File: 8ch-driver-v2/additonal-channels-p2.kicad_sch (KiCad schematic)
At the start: 42 parts, among them Q1 2N7002E, U1 DRV104PWP

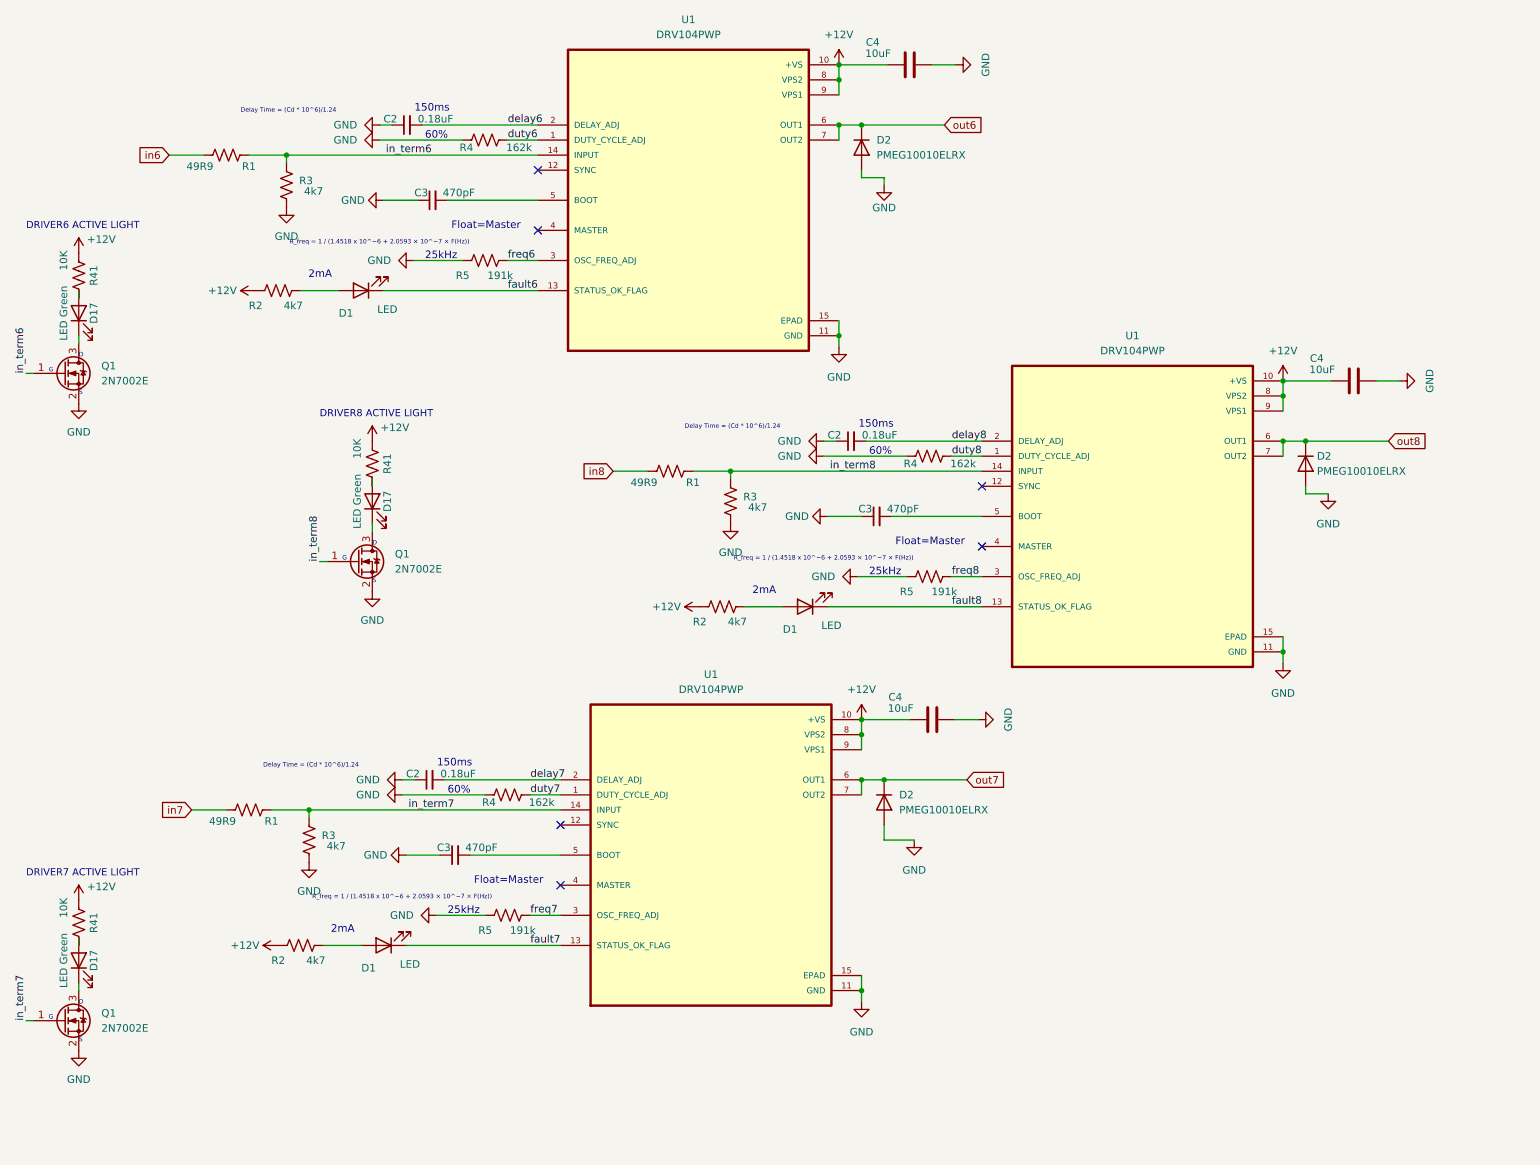
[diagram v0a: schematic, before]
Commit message: added 8 more channels and an FTDH chip
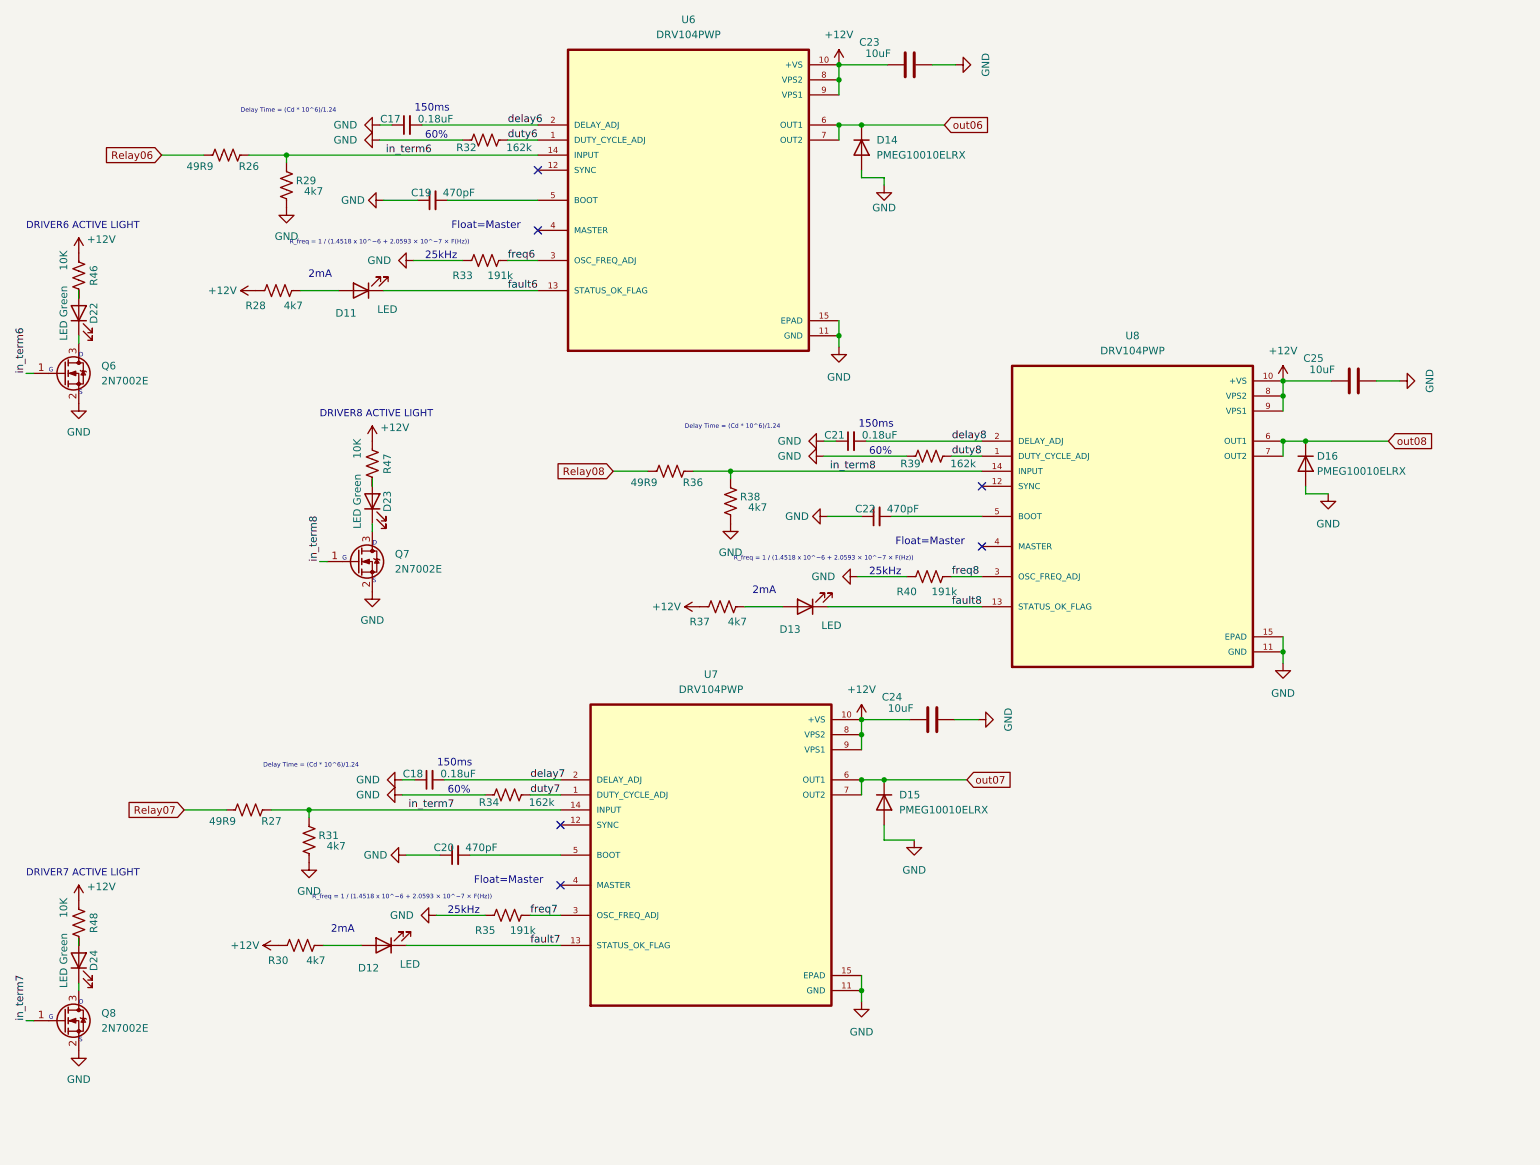
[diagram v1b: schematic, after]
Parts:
- renumbered C2 to C17, C2 to C18, C3 to C19, C3 to C20, C2 to C21, C3 to C22, C4 to C23, C4 to C24, C4 to C25, D1 to D11, D1 to D12, D1 to D13, D2 to D14, D2 to D15, D2 to D16, D17 to D22, D17 to D23, D17 to D24, Q1 to Q6, Q1 to Q7, Q1 to Q8, R1 to R26, R1 to R27, R2 to R28, R3 to R29, R2 to R30, R3 to R31, R4 to R32, R5 to R33, R4 to R34, R5 to R35, R1 to R36, R2 to R37, R3 to R38, R4 to R39, R5 to R40, R41 to R46, R41 to R47, R41 to R48, U1 to U6, U1 to U7, U1 to U8
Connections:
- net in6 renamed Relay06
- net in7 renamed Relay07
- net in8 renamed Relay08
- net out6 renamed out06
- net out7 renamed out07
- net out8 renamed out08
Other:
- title: (none) -> 16 Channel PWM Solenoid Driver - USB

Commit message: progress
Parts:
- removed C19, C22: 470pF, Capacitor_SMD:C_1206_3216Metric, symbol Device:C_Small
- removed C23, C24: 10uF, Capacitor_SMD:C_1210_3225Metric, symbol Device:C
- removed D12: LED, LED_SMD:LED_0805_2012Metric, symbol Device:LED
- removed D15: PMEG10010ELRX, Diode_SMD:Nexperia_CFP3_SOD-123W, symbol Device:D
- added C19, C22: 10uF, Capacitor_SMD:C_1210_3225Metric, symbol Device:C
- added C23: 0.18uF, Capacitor_SMD:C_1206_3216Metric, symbol Device:C_Small
- added C24: 470pF, Capacitor_SMD:C_1206_3216Metric, symbol Device:C_Small
- added D12: PMEG10010ELRX, Diode_SMD:Nexperia_CFP3_SOD-123W, symbol Device:D
- added D15: LED, LED_SMD:LED_0805_2012Metric, symbol Device:LED
- C18, C21: value 0.18uF -> 470pF; Mfg KYOCERA AVX -> Kemet; PartNum 08053C184KAT2A -> C0805C471K5RAC7800
- C20: value 470pF -> 0.18uF; Mfg Kemet -> KYOCERA AVX; PartNum C0805C471K5RAC7800 -> 08053C184KAT2A
- R27: value 49R9 -> 4k7; PartNum RC0805FR-0749R9L -> RC0805JR-074K7L
- R29: value 4k7 -> 162k; PartNum RC0805JR-074K7L -> RC0805FR-07162KL
- R30: value 4k7 -> 191k; PartNum RC0805JR-074K7L -> RC0805FR-07191KL
- R31: value 4k7 -> 49R9; PartNum RC0805JR-074K7L -> RC0805FR-0749R9L
- R32: value 162k -> 4k7; PartNum RC0805FR-07162KL -> RC0805JR-074K7L
- R33: value 191k -> 4k7; PartNum RC0805FR-07191KL -> RC0805JR-074K7L
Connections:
- net +12V: now also R27.1, R32.1, C19.1, C22.1; no longer R28.1, R30.1
- net GND: now also R28.1, R30.1, C19.2, C22.2, C23.1, C24.1, D12.2 (A); no longer R31.1, R32.1
- net Relay07: now also R31.1; no longer R27.1
- net delay7: now also C20.2; no longer C18.2
- net delay8: now also C23.2; no longer C21.2
- net duty6: now also R29.2; no longer R32.2
- net fault7: now also D13.1 (K)
- net fault8: now also D15.1 (K); no longer D13.1 (K)
- net freq6: now also R30.2; no longer R33.2
- net in_term6: no longer R26.2, R29.2, U6.14 (INPUT)
- net in_term7: now also Q7.1 (G); no longer Q8.1 (G), R27.2, R31.2, U7.14 (INPUT)
- net in_term8: now also Q8.1 (G); no longer Q7.1 (G), R36.2, R38.2, U8.14 (INPUT)
- net out06: now also D12.1 (K); no longer D14.1 (K)
- net out07: now also D14.1 (K)
- net at U7.5 (BOOT): now also C21.2; no longer C20.2
- net at U6.5 (BOOT): now also C18.2
- net at R37.2: now also D15.2 (A); no longer D13.2 (A)
- net at U8.5 (BOOT): now also C24.2
- net at Q8.3 (D): now also D23.1 (K); no longer D24.1 (K)
- net at Q7.3 (D): now also D24.1 (K); no longer D23.1 (K)
- net at D11.2 (A): now also R27.2; no longer R28.2
- new net: D13.2 (A), R32.2
- new net in_term5: R26.2, R28.2, R31.2, R33.2, R36.2, R38.2, U6.14 (INPUT), U7.14 (INPUT), U8.14 (INPUT)

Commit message: mucho mas progresso
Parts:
- removed C17, C20, C23: 0.18uF, Capacitor_SMD:C_1206_3216Metric, symbol Device:C_Small
- removed C19, C22, C25: 10uF, Capacitor_SMD:C_1210_3225Metric, symbol Device:C
- removed D11, D13, D15: LED, LED_SMD:LED_0805_2012Metric, symbol Device:LED
- removed D12, D14: PMEG10010ELRX, Diode_SMD:Nexperia_CFP3_SOD-123W, symbol Device:D
- removed D22: LED Green, LED_SMD:LED_0805_2012Metric, symbol Device:LED
- removed R26: 49R9, Resistor_SMD:R_1206_3216Metric, symbol Device:R_US
- removed R27, R28: 4k7, Resistor_SMD:R_1206_3216Metric, symbol Device:R_US
- removed R29: 162k, Resistor_SMD:R_1206_3216Metric, symbol Device:R_US
- removed R30: 191k, Resistor_SMD:R_1206_3216Metric, symbol Device:R_US
- added C17, C20, C23: 10uF, Capacitor_SMD:C_1210_3225Metric, symbol Device:C
- added C19, C22, C25: 470pF, Capacitor_SMD:C_1206_3216Metric, symbol Device:C_Small
- added D17, D20: LED Green, LED_SMD:LED_0805_2012Metric, symbol Device:LED
- added D18, D21: LED, LED_SMD:LED_0805_2012Metric, symbol Device:LED
- added D19, D22: PMEG10010ELRX, Diode_SMD:Nexperia_CFP3_SOD-123W, symbol Device:D
- added R41: 191k, Resistor_SMD:R_1206_3216Metric, symbol Device:R_US
- added R42: 4k7, Resistor_SMD:R_1206_3216Metric, symbol Device:R_US
- added R43: 10K, Resistor_SMD:R_1206_3216Metric, symbol Device:R_US
- added R44: 162k, Resistor_SMD:R_1206_3216Metric, symbol Device:R_US
- added R45: 49R9, Resistor_SMD:R_1206_3216Metric, symbol Device:R_US
- C18, C21, C24: value 470pF -> 0.18uF; Mfg Kemet -> KYOCERA AVX; PartNum C0805C471K5RAC7800 -> 08053C184KAT2A
- D24: value LED Green -> LED
- R31: value 49R9 -> 10K; PartNum RC0805FR-0749R9L -> RC0805FR-07162KL
- R32, R38: value 4k7 -> 162k; PartNum RC0805JR-074K7L -> RC0805FR-07162KL
- R33: value 4k7 -> 49R9; PartNum RC0805JR-074K7L -> RC0805FR-0749R9L
- R34: value 162k -> 4k7; PartNum RC0805FR-07162KL -> RC0805JR-074K7L
- R36: value 49R9 -> 4k7; PartNum RC0805FR-0749R9L -> RC0805JR-074K7L
- R37: value 4k7 -> 10K; PartNum RC0805JR-074K7L -> RC0805FR-07162KL
- R39: value 162k -> 49R9; PartNum RC0805FR-07162KL -> RC0805FR-0749R9L
- R40: value 191k -> 4k7; PartNum RC0805FR-07191KL -> RC0805JR-074K7L
- R46, R48: value 10K -> 4k7; PartNum RC0805FR-07162KL -> RC0805JR-074K7L
- R47: value 10K -> 191k; PartNum RC0805FR-07162KL -> RC0805FR-07191KL
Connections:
- net duty6 is gone; now on net duty06: U6.1 (DUTY_CYCLE_ADJ)
- net in_term8 is gone; now on net in_term08: Q8.1 (G)
- net +12V: now also R31.1, R36.1, C17.1, C20.1, C23.1, R42.1, R43.1; no longer R32.1, R46.1, R47.1
- net GND: now also R32.1, R46.1, R47.1, C17.2, C19.1, C20.2, C22.1, C23.2, C25.1, D19.2 (A), D22.2 (A), R41.1, R44.1; no longer R33.1, R39.1
- net Relay06: now also R33.1
- net Relay07: now also R39.1; no longer R31.1
- net Relay08: now also R45.1; no longer R36.1
- net out06: now also D16.1 (K)
- net out07: now also D19.1 (K)
- net out08: now also D22.1 (K); no longer D16.1 (K)
- net at R37.2: now also D20.2 (A)
- net at D23.2 (A): now also R43.2; no longer R47.2
- net duty06: now reaches R32.2
- net at U6.5 (BOOT): now also C19.2; no longer C18.2
- net in_term08: now reaches R46.2
- net in_term08: now also U8.14 (INPUT), R45.2
- net at U8.5 (BOOT): now also C25.2; no longer C24.2
- net at U7.5 (BOOT): now also C22.2; no longer C21.2
- net at Q6.3 (D): now also D17.1 (K)
- net at Q7.3 (D): now also D20.1 (K); no longer D24.1 (K)
- net delay6 renamed delay06
- net delay06: now also C18.2
- net delay7 renamed delay07
- net delay07: now also C21.2
- net delay8 renamed delay08
- net delay08: now also C24.2
- net duty7 renamed duty07
- net duty07: now also R38.2; no longer R34.2
- net duty8 renamed duty08
- net duty08: now also R44.2; no longer R39.2
- net fault6 renamed fault06
- net fault06: now also D18.1 (K)
- net fault7 renamed fault07
- net fault07: now also D21.1 (K)
- net fault8 renamed fault08
- net fault08: now also D24.1 (K)
- net freq6 renamed freq06
- net freq06: now also R35.2
- net freq7 renamed freq07
- net freq07: now also R41.2; no longer R35.2
- net freq8 renamed freq08
- net freq08: now also R47.2; no longer R40.2
- removed net in_term5: R31.2, R33.2, R36.2, R38.2, U6.14 (INPUT), U7.14 (INPUT), U8.14 (INPUT)
- net in_term6 renamed in_term06
- net in_term06: now also R33.2, R34.2, U6.14 (INPUT)
- net in_term7 renamed in_term07
- net in_term07: now also R39.2, R40.2, U7.14 (INPUT)
- new net: D21.2 (A), R42.2
- new net: D17.2 (A), R31.2
- new net: D18.2 (A), R36.2
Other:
- note removed: "DRIVER7 ACTIVE LIGHT"
- note removed: "DRIVER8 ACTIVE LIGHT"
